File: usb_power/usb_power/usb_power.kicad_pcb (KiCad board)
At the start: 2 copper layers, 24.1 x 21 mm, 8 parts, among them J1 USB_B_Micro, J2 Conn_01x02, J3 Conn_01x03, J4 Conn_01x04, U1 TLV75533PDBV

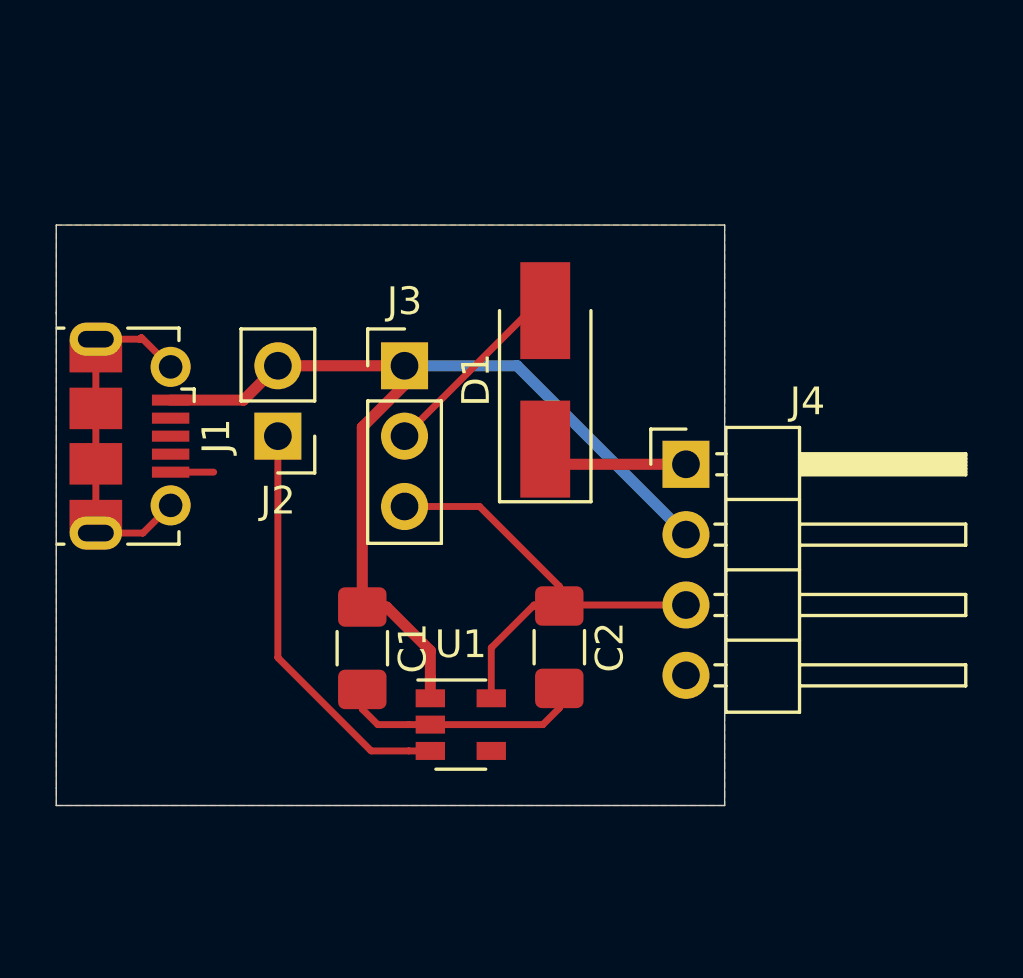
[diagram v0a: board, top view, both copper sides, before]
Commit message: Added USB communication to USB Power Board
Added FT232RL USB-to-UART Transceiver as debug port for TARGET board.
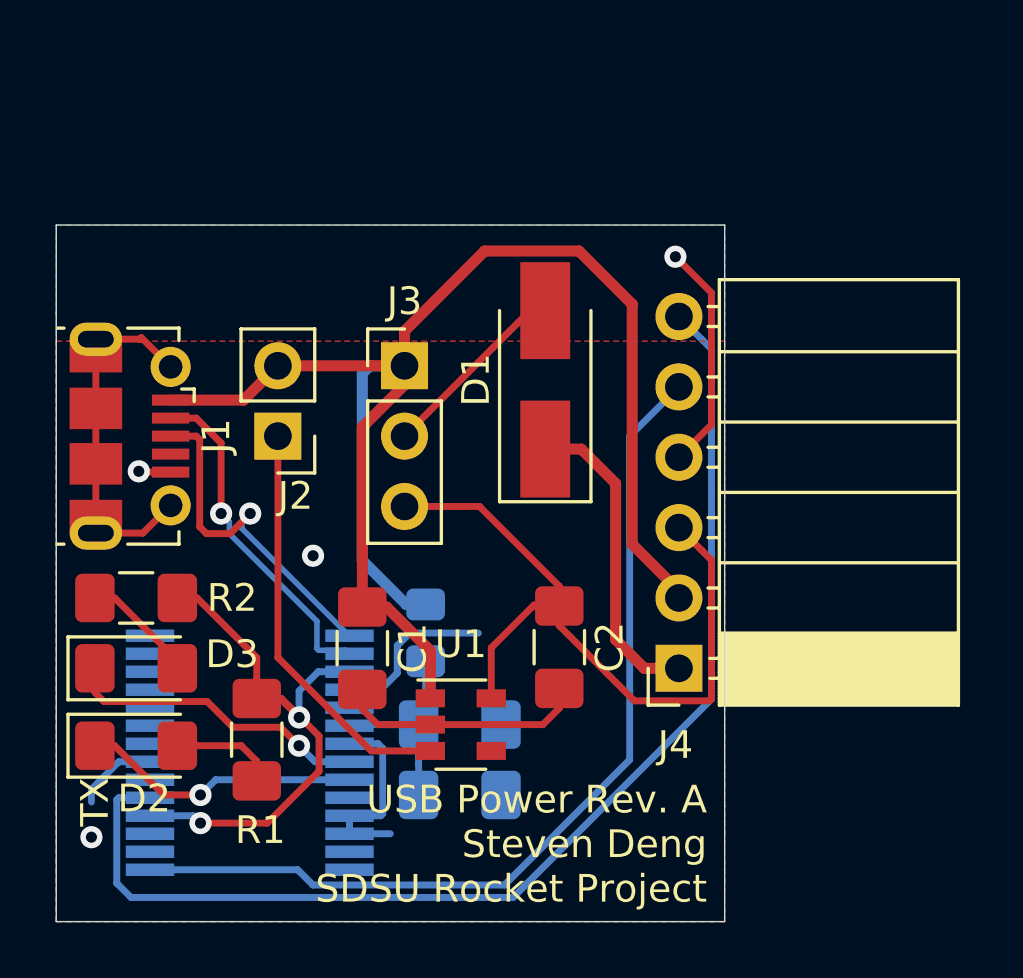
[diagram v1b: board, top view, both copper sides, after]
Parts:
- added C3: 10uF, Capacitor_SMD:C_1206_3216Metric_Pad1.42x1.75mm_HandSolder, B.Cu at (165.1, 108.2)
- added C4: 0.1uF, Capacitor_SMD:C_1206_3216Metric_Pad1.42x1.75mm_HandSolder, B.Cu at (165.1, 105.7)
- added D2: LED, LED_SMD:LED_1206_3216Metric_Pad1.42x1.75mm_HandSolder, F.Cu at (153.4, 106.4)
- added D3: LED, LED_SMD:LED_1206_3216Metric_Pad1.42x1.75mm_HandSolder, F.Cu at (153.4, 103.6)
- added FB1: Ferrite_Bead_Small, Resistor_SMD:R_0805_2012Metric_Pad1.15x1.40mm_HandSolder, B.Cu at (163.8, 102.4)
- added R1: 330, Resistor_SMD:R_1206_3216Metric_Pad1.42x1.75mm_HandSolder, F.Cu at (157.7, 106.2)
- added R2: 330, Resistor_SMD:R_1206_3216Metric_Pad1.42x1.75mm_HandSolder, F.Cu at (153.4, 101.1)
- added U2: FT232RL, Package_SO:SSOP-28_5.3x10.2mm_P0.65mm, B.Cu at (157.5, 106.7)
- J4: value Conn_01x04 -> Conn_01x06; footprint Connector_PinHeader_2.54mm:PinHeader_1x04_P2.54mm_Horizontal -> Connector_PinSocket_2.54mm:PinSocket_1x06_P2.54mm_Horizontal
- moved J4 7.37 mm to (173.0, 103.6), turned to 180 degrees
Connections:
- J1 pad 2: Net-(J1-Pad2) -> /USB_D-
- J1 pad 3: Net-(J1-Pad3) -> /USB_D+
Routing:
- net /TARGET_TX: track 0.00 -> 43.2 mm
- net /TARGET_RX: track 0.00 -> 33.6 mm
- net GND: track 10.6 -> 34.7 mm, vias 0 -> 4
- net +5V: track 35.8 -> 57.2 mm
- net /FT232_3V3_OUT: track 0.00 -> 21.2 mm, vias 0 -> 2
- net /USB_D+: track 0.00 -> 12.6 mm, vias 0 -> 1
- net /USB_D-: track 0.00 -> 12.3 mm, vias 0 -> 1
- net /RXLED: track 0.00 -> 11.1 mm, vias 0 -> 1
- net /TXLED: track 0.00 -> 10.2 mm, vias 0 -> 1
- net +3V3: track 17.0 -> 26.5 mm
- net Net-(C3-Pad1): track 0.00 -> 7.44 mm
- net VCC: track 5.31 -> 11.4 mm
- net Net-(D3-Pad2): track 0.00 -> 4.19 mm
- net Net-(D2-Pad2): track 0.00 -> 3.81 mm
- added copper zone on B.Cu, net GND
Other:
- board size 24.1 x 21 mm -> 24.1 x 25.1 mm
- board text added: "TX"
- board text added: "USB Power Rev. A Steven Deng SDSU Rocket Project"

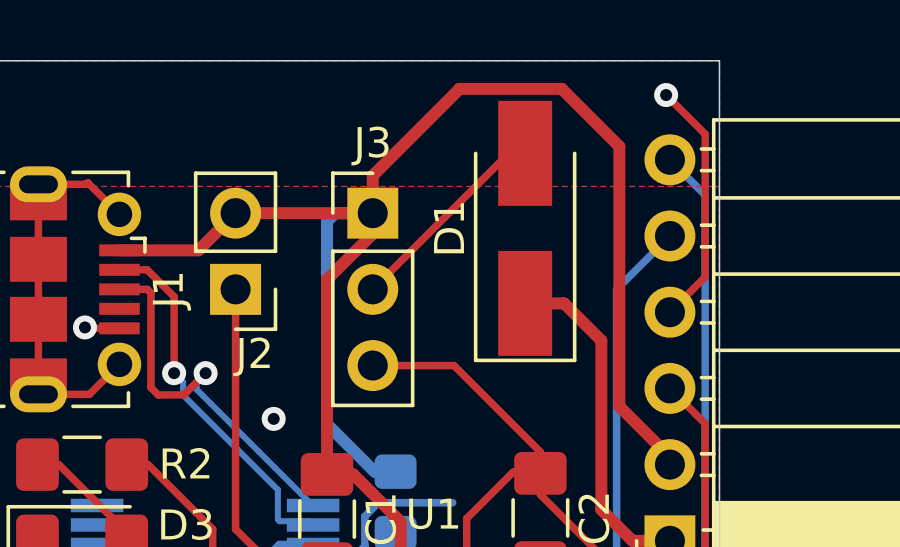
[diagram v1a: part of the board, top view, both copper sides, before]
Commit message: Added logo to board layout
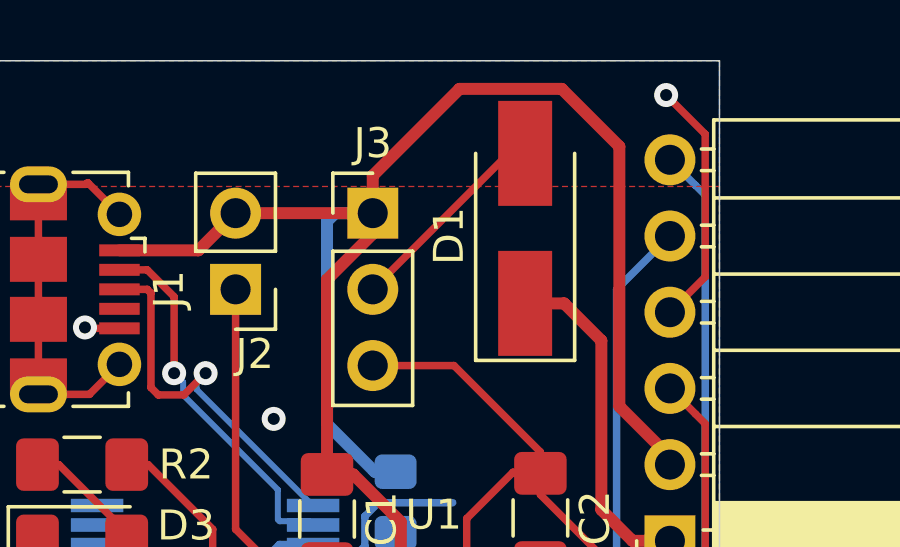
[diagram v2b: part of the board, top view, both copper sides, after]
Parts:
- added G***: LOGO, SDSURP:sdsu_kicad_logo, B.Cu at (168.1, 90.7)

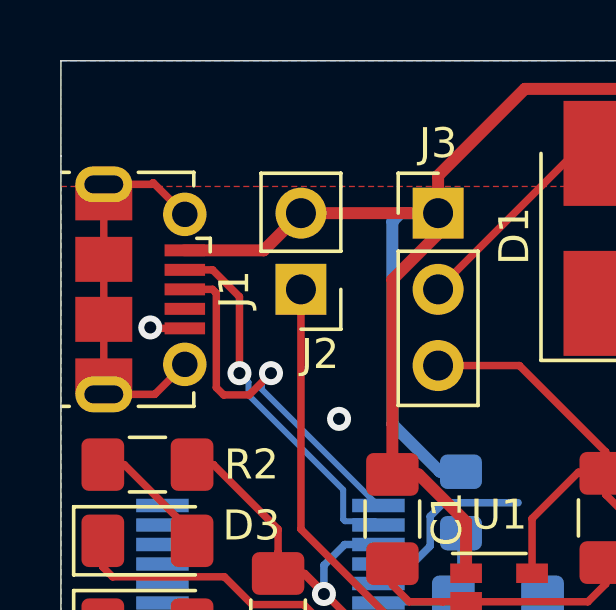
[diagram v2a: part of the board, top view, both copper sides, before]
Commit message: Prepared PCB for manufacture
Replaced USB micro connector with one that is in stock.
Exported gerbers.
Added Digikey part numbers to schematic symbols.
Generated BOM for Digikey.
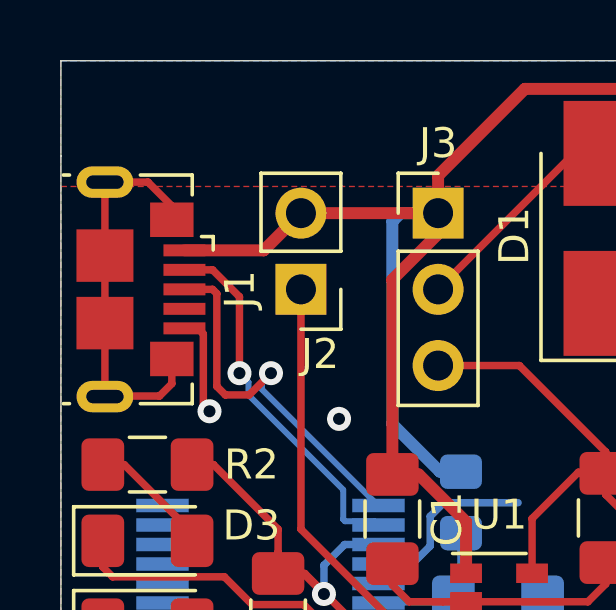
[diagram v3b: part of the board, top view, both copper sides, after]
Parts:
- removed G***: LOGO, SDSURP:sdsu_kicad_logo
- J1: footprint Connector_USB:USB_Micro-B_Molex-105017-0001 -> Connector_USB:USB_Micro-B_GCT_USB3076-30-A
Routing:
- net GND: track 34.7 -> 37.0 mm
- net Net-(J1-Pad6): track 12.7 -> 13.4 mm

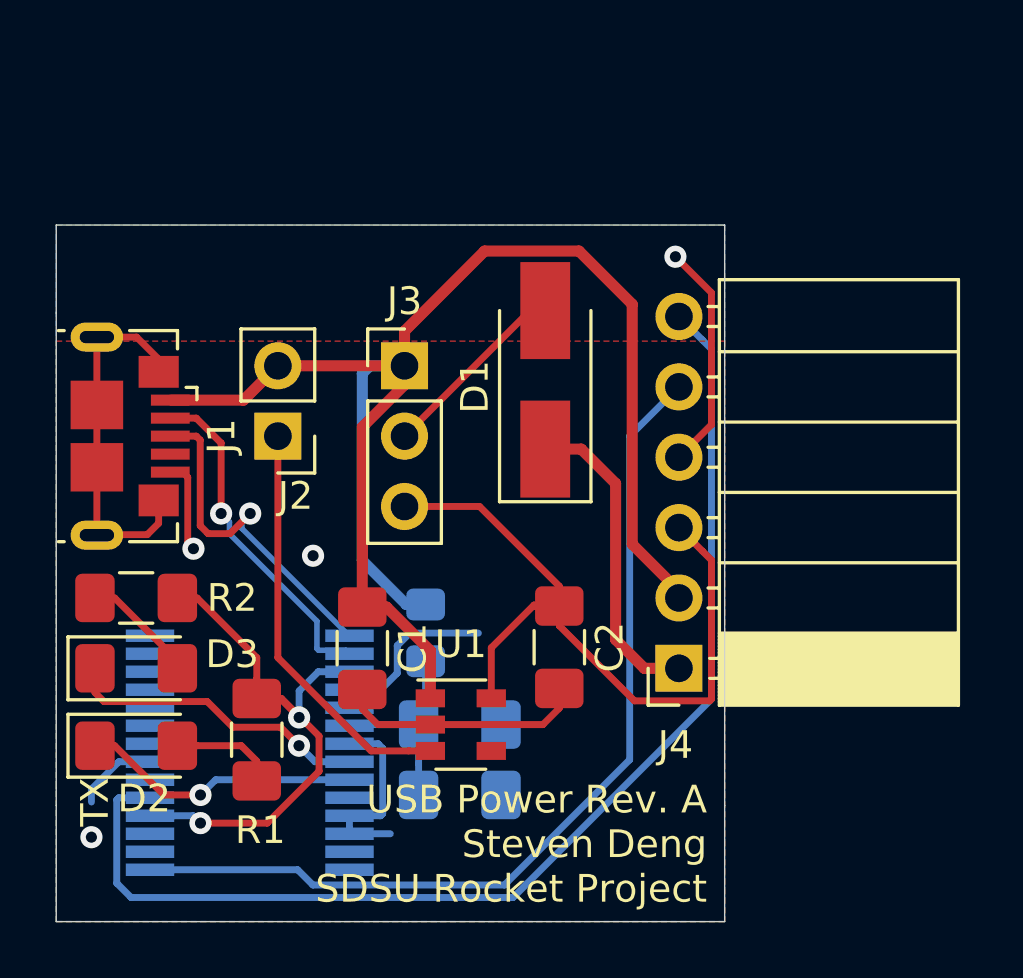
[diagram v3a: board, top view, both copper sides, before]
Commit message: Added more silkscreen text to PCB
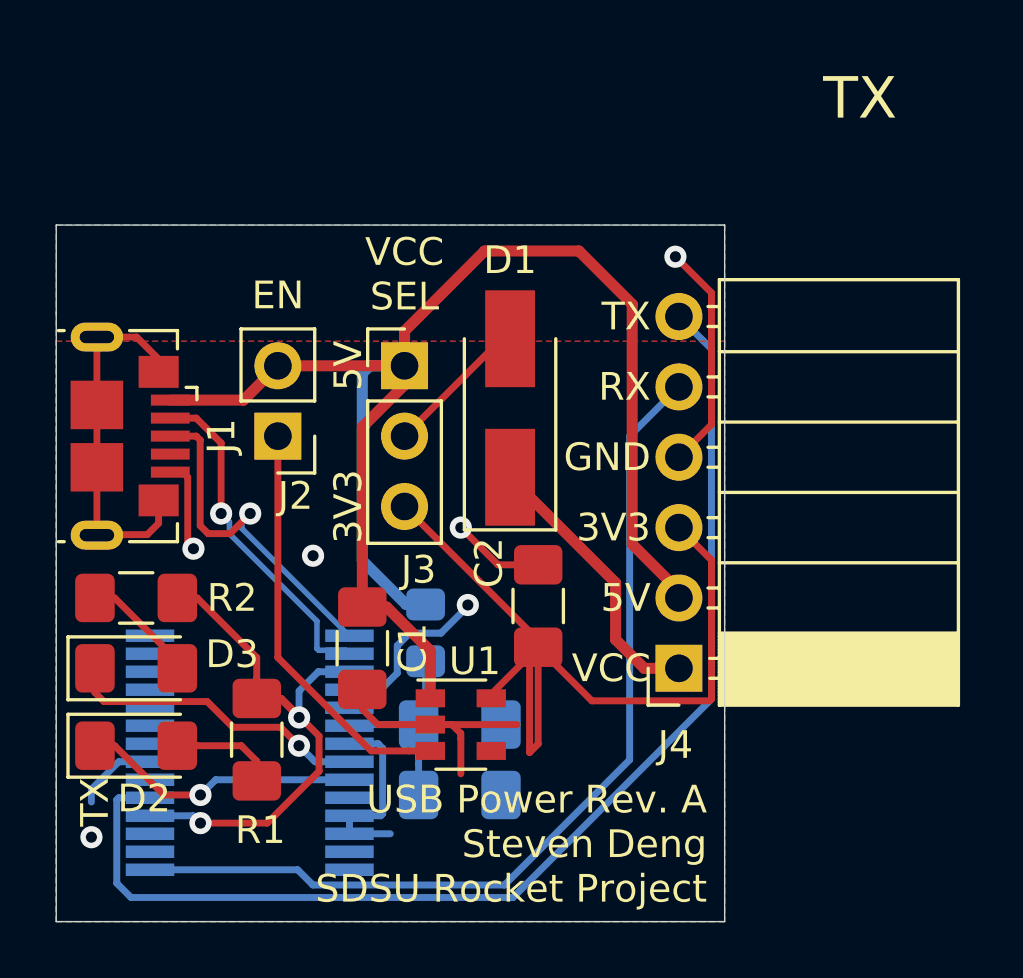
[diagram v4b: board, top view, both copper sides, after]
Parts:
- moved C2 1.67 mm to (167.9, 101.4), turned to 90 degrees
- moved D1 1.63 mm to (166.9, 94.2)
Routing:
- net +3V3: track 26.5 -> 31.0 mm
- net GND: track 37.0 -> 40.6 mm, vias 4 -> 6
- net Net-(D1-Pad2): track 6.96 -> 5.27 mm
- net VCC: track 11.4 -> 10.2 mm
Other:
- board text added: "3V3"
- board text added: "5V"
- board text added: "EN"
- board text added: "GND"
- board text added: "RX"
- board text added: "VCC"
- board text added: "VCC SEL"
